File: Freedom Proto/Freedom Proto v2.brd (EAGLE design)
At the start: 100 x 100 mm, 8 parts, among them X1 0446200002

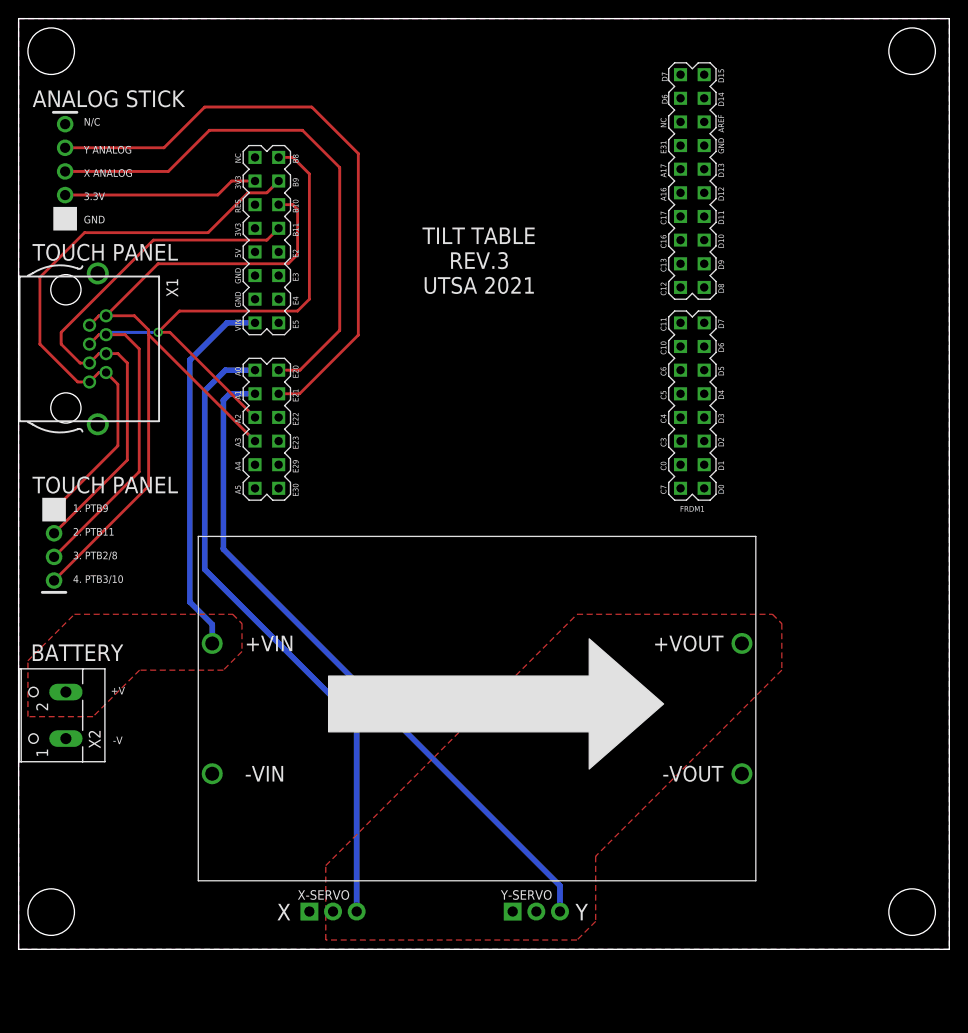
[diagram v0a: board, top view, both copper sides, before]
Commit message: ATmega328 reference design
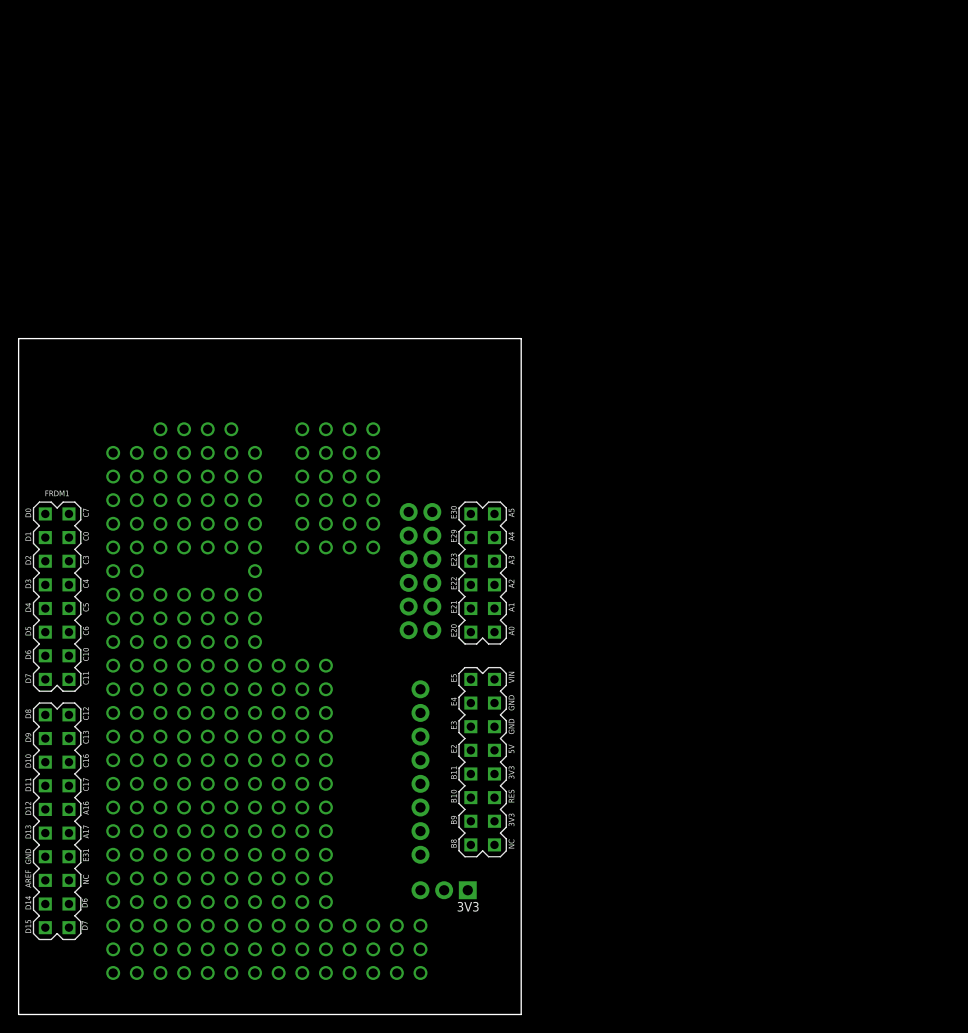
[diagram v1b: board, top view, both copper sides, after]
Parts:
- removed JS: PINS_5SILK, nolan-utsa:PCB_5
- removed U$3: PINS_4SILK, nolan-utsa:PCB_4
- removed U$4: MODULE-DCDC, nolan-utsa:DCDC_CONVERTER_MH
- removed X-SERVO, Y-SERVO: PINS_3_2.54, nolan-utsa:PINS_3
- removed X1: 0446200002, con-molex:0446200002
- removed X2: (no value), con-wago-500:W237-102
- added 3V3: PINS_3_2.54, nolan-utsa:PINS_3
- added B0, E21, J9.12, PTB1, PTB10, PTB11, PTB2, PTB3, PTB8, PTB9, PTC1, PTC2, PTE2, PTE22, PTE23, PTE29, PTE3, PTE30, PTE4, PTE5: PINS_1, nolan-utsa:PINS_1_TEXT
- moved FRDM1 44.4 mm to (27.0, 29.0), turned to 0 degrees
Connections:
- removed net 3.3V: FRDM1.3V3, JS.P$2
- removed net 5-9V: FRDM1.VIN, U$4.+VIN, X2.2
- removed net BLU: FRDM1.PTB11, U$3.P$2, X1.3, X1.4
- removed net BRN: FRDM1.A3, FRDM1.PTB10, U$3.P$4, X1.7, X1.8
- removed net GND: FRDM1.GND0, FRDM1.GND1, FRDM1.GND2, JS.P$1, U$4.-VIN, U$4.-VOUT, X-SERVO.1, X1.S@1, X1.S@2, X2.1, Y-SERVO.1
- removed net GRN: FRDM1.A2, FRDM1.PTB8, U$3.P$3, X1.5, X1.6
- removed net N$2: U$4.+VOUT, X-SERVO.2, Y-SERVO.2
- removed net ORG: FRDM1.PTB9, U$3.P$1, X1.1, X1.2
- removed net PTB0: FRDM1.A0, X-SERVO.3
- removed net PTB1: FRDM1.A1, Y-SERVO.3
- removed net X_ANA: FRDM1.PTE20, JS.P$3
- removed net Y_ANA: FRDM1.PTE21, JS.P$4
- new net N$21: B0.1, FRDM1.A0
- new net N$23: FRDM1.A1, PTB1.1
- new net N$25: FRDM1.A2, PTB2.1
- new net N$27: FRDM1.A3, PTB3.1
- new net N$295: 3V3.1, 3V3.2, 3V3.3, FRDM1.3V3
- new net N$298: FRDM1.PTB8, PTB8.1
- new net N$299: FRDM1.PTB9, PTB9.1
- new net N$302: FRDM1.PTB10, PTB10.1
- new net N$303: FRDM1.PTB11, PTB11.1
- new net N$306: FRDM1.PTE2, PTE2.1
- new net N$308: FRDM1.PTE3, PTE3.1
- new net N$310: FRDM1.PTE4, PTE4.1
- new net N$312: FRDM1.PTE5, PTE5.1
- new net N$49: FRDM1.A5, PTC1.1
- new net N$50: FRDM1.PTE20, J9.12.1
- new net N$51: E21.1, FRDM1.PTE21
- new net N$52: FRDM1.PTE22, PTE22.1
- new net N$53: FRDM1.PTE23, PTE23.1
- new net N$54: FRDM1.PTE29, PTE29.1
- new net N$55: FRDM1.PTE30, PTE30.1
- new net N$56: FRDM1.A4, PTC2.1
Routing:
- net GRN: track 88.2 -> 0.00 mm, vias 1 -> 0
- net BRN: track 85.1 -> 0.00 mm
- net PTB1: track 73.6 -> 0.00 mm
- net PTB0: track 69.0 -> 0.00 mm
- net Y_ANA: track 66.1 -> 0.00 mm
- net ORG: track 64.4 -> 0.00 mm
- net BLU: track 59.6 -> 0.00 mm
- net X_ANA: track 58.8 -> 0.00 mm
- net 5-9V: track 40.1 -> 0.00 mm
- net 3.3V: track 21.0 -> 0.00 mm
- removed copper zone on layer 1, net 5-9V
- removed copper zone on layer 1, net GND
- removed copper zone on layer 16, net GND
- removed copper zone on layer 1, net N$2
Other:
- board size 100 x 100 mm -> 54 x 72.6 mm
- board text removed: "+V"
- board text removed: "-V"
- board text removed: "1. PTB9"
- board text removed: "2. PTB11"
- board text removed: "3. PTB2/8"
- board text removed: "3.3V"
- board text removed: "4. PTB3/10"
- board text removed: "ANALOG STICK"
- board text removed: "BATTERY"
- board text removed: "GND"
- board text removed: "N/C"
- board text removed: "TILT TABLE REV.3 UTSA 2021"
- board text removed: "TOUCH PANEL"
- board text removed: "X"
- board text removed: "X ANALOG"
- board text removed: "Y"
- board text removed: "Y ANALOG"
